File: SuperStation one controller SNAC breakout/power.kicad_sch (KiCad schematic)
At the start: 11 parts, among them U1 SN74LVC1G3157, U2 SN74LVC1G3157, U3 SN74LVC1G3157, U4 SN74LVC1G3157, U5 SN74LVC1G3157, U6 SN74LVC1G3157, U7 SN74LVC1G3157, U8 NCP1117-5.0_SOT223

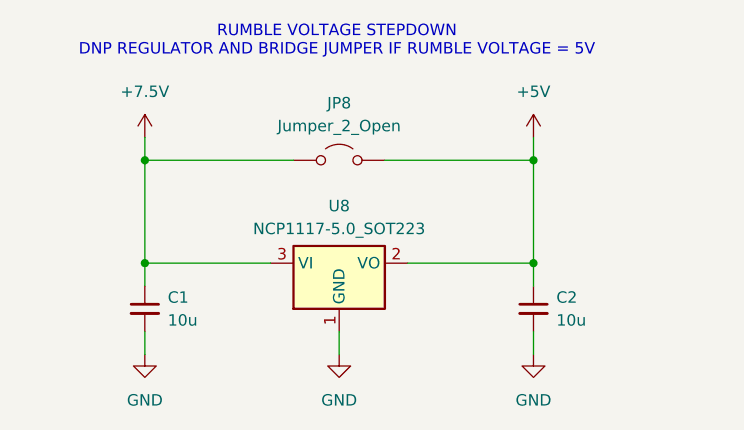
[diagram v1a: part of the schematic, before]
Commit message: replaced voltage regulator with a cheaper and smaller alternative. The same that is on all opensource SNAC adapters.
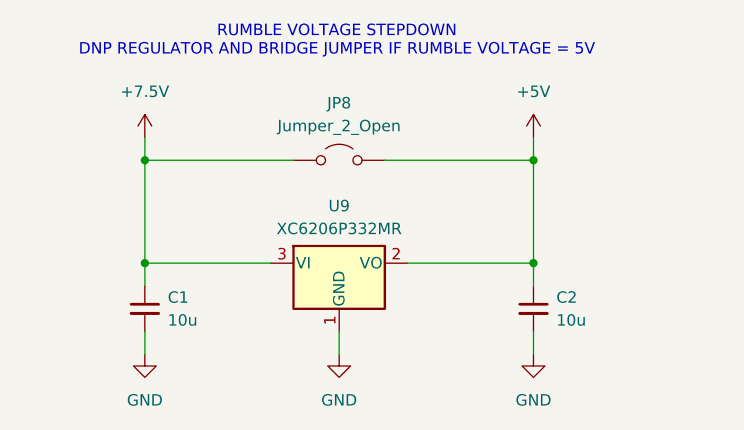
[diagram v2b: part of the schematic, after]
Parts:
- removed U8: NCP1117-5.0_SOT223, Package_TO_SOT_SMD:SOT-223-3_TabPin2, symbol Regulator_Linear:NCP1117-5.0_SOT223
- added U9: XC6206P332MR, Package_TO_SOT_SMD:SOT-23-3, symbol Regulator_Linear:XC6206PxxxMR
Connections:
- net +5V: now also U9.2 (VO)
- net +7.5V: now also U9.3 (VI)
- net GND: now also U9.1 (GND)
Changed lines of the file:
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@@
+	)
+	(symbol
+		(lib_id "Regulator_Linear:XC6206PxxxMR")
+		(at 66.04 68.58 0)
+		(unit 1)
+		(exclude_from_sim no)
+		(in_bom yes)
+		(on_board yes)
+		(dnp no)
+		(fields_autoplaced yes)
+		(property "Reference" "U9"
+			(at 66.04 62.23 0)
+			(effects
+				(font
+					(size 1.27 1.27)
+				)
+			)
+		)
+		(property "Value" "XC6206P332MR"
+			(at 66.04 64.77 0)
+			(effects
+				(font
+					(size 1.27 1.27)
+				)
+			)
+		)
+		(property "Footprint" "Package_TO_SOT_SMD:SOT-23-3"
+			(at 66.04 62.865 0)
+			(effects
+				(font
+					(size 1.27 1.27)
+					(italic yes)
+				)
+				(hide yes)
+			)
+		)
+		(property "Datasheet" "https://www.torexsemi.com/file/xc6206/XC6206.pdf"
+			(at 66.04 68.58 0)
+			(effects
+				(font
+					(size 1.27 1.27)
+				)
+				(hide yes)
+			)
+		)
+		(property "Description" "Positive 60-250mA Low Dropout Regulator, Fixed Output, SOT-23"
+			(at 66.04 68.58 0)
+			(effects
+				(font
+					(size 1.27 1.27)
+				)
+				(hide yes)
+			)
+		)
+		(pin "1"
+		)
+		(pin "2"
+		)
+		(pin "3"
+		)
+		(instances
+			(project ""
+				(path "/cbd92933-d20e-42b7-906c-813e5f34c94a/9f4e6185-3dfc-4ab7-b065-b07efc3c4f4a"
+					(reference "U9")
+					(unit 1)
+				)
+			)
+		)
 	)
 	(symbol
@@
 				)
 			)
-		)
-	)
-	(symbol
-		(lib_id "Regulator_Linear:NCP1117-5.0_SOT223")
-		(at 66.04 68.58 0)
-		(unit 1)
-		(exclude_from_sim no)
-		(in_bom yes)
-		(on_board yes)
-		(dnp no)
-		(fields_autoplaced yes)
-		(property "Reference" "U8"
-			(at 66.04 62.23 0)
-			(effects
-				(font
-					(size 1.27 1.27)
-				)
-			)
-		)
-		(property "Value" "NCP1117-5.0_SOT223"
-			(at 66.04 64.77 0)
-			(effects
-				(font
-					(size 1.27 1.27)
-				)
-			)
-		)
-		(property "Footprint" "Package_TO_SOT_SMD:SOT-223-3_TabPin2"
-			(at 66.04 63.5 0)
-			(effects
-				(font
-					(size 1.27 1.27)
-				)
-				(hide yes)
-			)
-		)
-		(property "Datasheet" "http://www.onsemi.com/pub_link/Collateral/NCP1117-D.PDF"
-			(at 68.58 74.93 0)
-			(effects
-				(font
-					(size 1.27 1.27)
-				)
-				(hide yes)
-			)
-		)
-		(property "Description" "1A Low drop-out regulator, Fixed Output 5V, SOT-223"
-			(at 66.04 68.58 0)
-			(effects
-				(font
-					(size 1.27 1.27)
-				)
-				(hide yes)
-			)
-		)
-		(pin "1"
-		)
-		(pin "2"
-		)
-		(pin "3"
-		)
-		(instances
-			(project "SuperStation one controller SNAC breakout"
-				(path "/cbd92933-d20e-42b7-906c-813e5f34c94a/9f4e6185-3dfc-4ab7-b065-b07efc3c4f4a"
-					(reference "U8")
-					(unit 1)
-				)
-			)
